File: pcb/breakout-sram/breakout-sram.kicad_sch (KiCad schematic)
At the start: 6 parts, among them J1 FX18-120P-0.8SV20, J2 FX18-120S-0.8SV20, U1 IS61WV102416DBLL-10TLI

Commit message: [pcb] misc updates prior to ordder
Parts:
- J1: Digi-Key Part Number (none) -> H11865-ND; now not fitted
- J2: Digi-Key Part Number (none) -> H11867-ND; now not fitted
- U1: LCSC Part # (none) -> C1348726
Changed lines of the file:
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@@
 		(in_bom yes)
 		(on_board yes)
-		(dnp no)
+		(dnp yes)
 		(property "Reference" "J1"
 			(at 23.876 94.488 90)
@@
 		)
 		(property "Description" ""
+			(at 41.91 96.52 0)
+			(effects
+				(font
+					(size 1.27 1.27)
+				)
+				(hide yes)
+			)
+		)
+		(property "Digi-Key Part Number" "H11865-ND"
 			(at 41.91 96.52 0)
 			(effects
@@
 		(in_bom yes)
 		(on_board yes)
-		(dnp no)
+		(dnp yes)
 		(property "Reference" "J1"
 			(at 57.658 94.488 90)
@@
 		)
 		(property "Description" ""
+			(at 76.2 96.52 0)
+			(effects
+				(font
+					(size 1.27 1.27)
+				)
+				(hide yes)
+			)
+		)
+		(property "Digi-Key Part Number" "H11865-ND"
 			(at 76.2 96.52 0)
 			(effects
@@
 		(in_bom yes)
 		(on_board yes)
-		(dnp no)
+		(dnp yes)
 		(property "Reference" "J2"
 			(at 340.868 119.126 90)
@@
 		)
 		(property "Description" ""
+			(at 356.87 96.52 0)
+			(effects
+				(font
+					(size 1.27 1.27)
+				)
+				(hide yes)
+			)
+		)
+		(property "Digi-Key Part Number" "H11867-ND"
 			(at 356.87 96.52 0)
 			(effects
@@
 			)
 		)
+		(property "LCSC Part #" " C1348726"
+			(at 208.28 125.73 0)
+			(effects
+				(font
+					(size 1.27 1.27)
+				)
+				(hide yes)
+			)
+		)
 		(pin "23"
 		)
@@
 		(in_bom yes)
 		(on_board yes)
-		(dnp no)
+		(dnp yes)
 		(property "Reference" "J2"
 			(at 307.086 120.142 90)
@@
 		)
 		(property "Description" ""
+			(at 322.58 96.52 0)
+			(effects
+				(font
+					(size 1.27 1.27)
+				)
+				(hide yes)
+			)
+		)
+		(property "Digi-Key Part Number" "H11867-ND"
 			(at 322.58 96.52 0)
 			(effects
@@
 		(in_bom yes)
 		(on_board yes)
-		(dnp no)
+		(dnp yes)
 		(property "Reference" "J1"
 			(at 94.488 94.234 90)
@@
 		)
 		(property "Description" ""
+			(at 113.03 96.52 0)
+			(effects
+				(font
+					(size 1.27 1.27)
+				)
+				(hide yes)
+			)
+		)
+		(property "Digi-Key Part Number" "H11865-ND"
 			(at 113.03 96.52 0)
 			(effects
@@
 		(in_bom yes)
 		(on_board yes)
-		(dnp no)
+		(dnp yes)
 		(property "Reference" "J2"
 			(at 377.698 119.888 90)
@@
 			(at 393.7 96.52 0)
 			(effects
+				(font
+					(size 1.27 1.27)
+				)
+				(hide yes)
+			)
+		)
+		(property "Digi-Key Part Number" "H11867-ND"
+			(at 393.7 96.52 0)
+			(effects

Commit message: [sram] update with correct nets labels
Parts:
- J1, J2: now fitted
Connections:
- net AB_02: now also J1.5, U1.46 (A7); no longer J1.4, U1.47 (A6)
- net AB_03: now also J1.7, U1.44 (OE#); no longer J1.5, U1.46 (A7)
- net AB_04: now also J1.9, U1.40 (I/O14); no longer J1.6, U1.45 (A8)
- net AB_05: now also J1.4, U1.47 (A6); no longer J1.7, U1.44 (OE#)
- net AB_06: now also J1.6, U1.45 (A8); no longer J1.8, U1.41 (I/O15)
- net AB_07: now also J1.8, U1.41 (I/O15); no longer J1.9, U1.40 (I/O14)
- net BA_02: now also J1.65, J2.5; no longer J1.64, J2.4
- net BA_03: now also J1.67, J2.7; no longer J1.65, J2.5
- net BA_04: now also J1.69, J2.9; no longer J1.66, J2.6
- net BA_05: now also J1.64, J2.4; no longer J1.67, J2.7
- net BA_06: now also J1.66, J2.6; no longer J1.68, J2.8
- net BA_07: now also J1.68, J2.8; no longer J1.69, J2.9
- net CD_02: now also J1.15, U1.34 (I/O10); no longer J1.14, U1.35 (I/O11)
- net CD_03: now also J1.17, U1.32 (I/O8); no longer J1.15, U1.34 (I/O10)
- net CD_04: now also J1.19, U1.29 (A10); no longer J1.16, U1.33 (I/O9)
- net CD_05: now also J1.14, U1.35 (I/O11); no longer J1.17, U1.32 (I/O8)
- net CD_06: now also J1.16, U1.33 (I/O9); no longer J1.18, U1.30 (A9)
- net CD_07: now also J1.18, U1.30 (A9); no longer J1.19, U1.29 (A10)
- net DC_02: now also J1.75, J2.15; no longer J1.74, J2.14
- net DC_03: now also J1.77, J2.17; no longer J1.75, J2.15
- net DC_04: now also J1.79, J2.19; no longer J1.76, J2.16
- net DC_05: now also J1.74, J2.14; no longer J1.77, J2.17
- net DC_06: now also J1.76, J2.16; no longer J1.78, J2.18
- net DC_07: now also J1.78, J2.18; no longer J1.79, J2.19
- net EF_02: now also J1.25, U1.25 (A14); no longer J1.24, U1.26 (A13)
- net EF_03: now also J1.27, U1.2 (A3); no longer J1.25, U1.25 (A14)
- net EF_04: now also J1.29, U1.4 (A1); no longer J1.26, U1.1 (A4)
- net EF_05: now also J1.24, U1.26 (A13); no longer J1.27, U1.2 (A3)
- net EF_06: now also J1.26, U1.1 (A4); no longer J1.28, U1.3 (A2)
- net EF_07: now also J1.28, U1.3 (A2); no longer J1.29, U1.4 (A1)
- net FE_01: now also J1.90, J2.30; no longer J1.83, J2.23
- net FE_02: now also J1.88, J2.28; no longer J1.84, J2.24
- net FE_03: now also J1.86, J2.26; no longer J1.85, J2.25
- net FE_04: now also J1.84, J2.24; no longer J1.86, J2.26
- net FE_05: now also J1.89, J2.29; no longer J1.87, J2.27
- net FE_06: now also J1.87, J2.27; no longer J1.88, J2.28
- net FE_07: now also J1.85, J2.25; no longer J1.89, J2.29
- net FE_08: now also J1.83, J2.23; no longer J1.90, J2.30
- net GH_02: now also J1.33, U1.9 (I/O1); no longer J1.32, U1.8 (I/O0)
- net GH_03: now also J1.35, U1.11 (I/O3); no longer J1.33, U1.9 (I/O1)
- net GH_04: now also J1.37, U1.15 (I/O5); no longer J1.34, U1.10 (I/O2)
- net GH_05: now also J1.32, U1.8 (I/O0); no longer J1.35, U1.11 (I/O3)
- net GH_06: now also J1.34, U1.10 (I/O2); no longer J1.36, U1.14 (I/O4)
- net GH_07: now also J1.36, U1.14 (I/O4); no longer J1.37, U1.15 (I/O5)
- net HG_02: now also J1.93, J2.33; no longer J1.92, J2.32
- net HG_03: now also J1.95, J2.35; no longer J1.93, J2.33
- net HG_04: now also J1.97, J2.37; no longer J1.94, J2.34
- net HG_05: now also J1.92, J2.32; no longer J1.95, J2.35
- net HG_06: now also J1.94, J2.34; no longer J1.96, J2.36
- net HG_07: now also J1.96, J2.36; no longer J1.97, J2.37
- net IJ_02: now also J1.43, U1.20 (A19); no longer J1.42, U1.18 (WE#)
- net IJ_03: now also J1.45, U1.22 (A17); no longer J1.43, U1.20 (A19)
- net IJ_04: now also J1.47, U1.24 (A15); no longer J1.44, U1.21 (A18)
- net IJ_05: now also J1.42, U1.18 (WE#); no longer J1.45, U1.22 (A17)
- net IJ_06: now also J1.44, U1.21 (A18); no longer J1.46, U1.23 (A16)
- net IJ_07: now also J1.46, U1.23 (A16); no longer J1.47, U1.24 (A15)
- net JI_01: now also J1.108, J2.48; no longer J1.101, J2.41
- net JI_02: now also J1.106, J2.46; no longer J1.102, J2.42
- net JI_03: now also J1.104, J2.44; no longer J1.103, J2.43
- net JI_04: now also J1.102, J2.42; no longer J1.104, J2.44
- net JI_05: now also J1.107, J2.47; no longer J1.105, J2.45
- net JI_06: now also J1.105, J2.45; no longer J1.106, J2.46
- net JI_07: now also J1.103, J2.43; no longer J1.107, J2.47
- net JI_08: now also J1.101, J2.41; no longer J1.108, J2.48
- net KL_02: now also J1.53, J2.113; no longer J1.52, J2.112
- net KL_03: now also J1.55, J2.115; no longer J1.53, J2.113
- net KL_04: now also J1.57, J2.117; no longer J1.54, J2.114
- net KL_05: now also J1.52, J2.112; no longer J1.55, J2.115
- net KL_06: now also J1.54, J2.114; no longer J1.56, J2.116
- net KL_07: now also J1.56, J2.116; no longer J1.57, J2.117
- net LK_02: now also J1.113, J2.53; no longer J1.112, J2.52
- net LK_03: now also J1.115, J2.55; no longer J1.113, J2.53
- net LK_04: now also J1.117, J2.57; no longer J1.114, J2.54
- net LK_05: now also J1.112, J2.52; no longer J1.115, J2.55
- net LK_06: now also J1.114, J2.54; no longer J1.116, J2.56
- net LK_07: now also J1.116, J2.56; no longer J1.117, J2.57

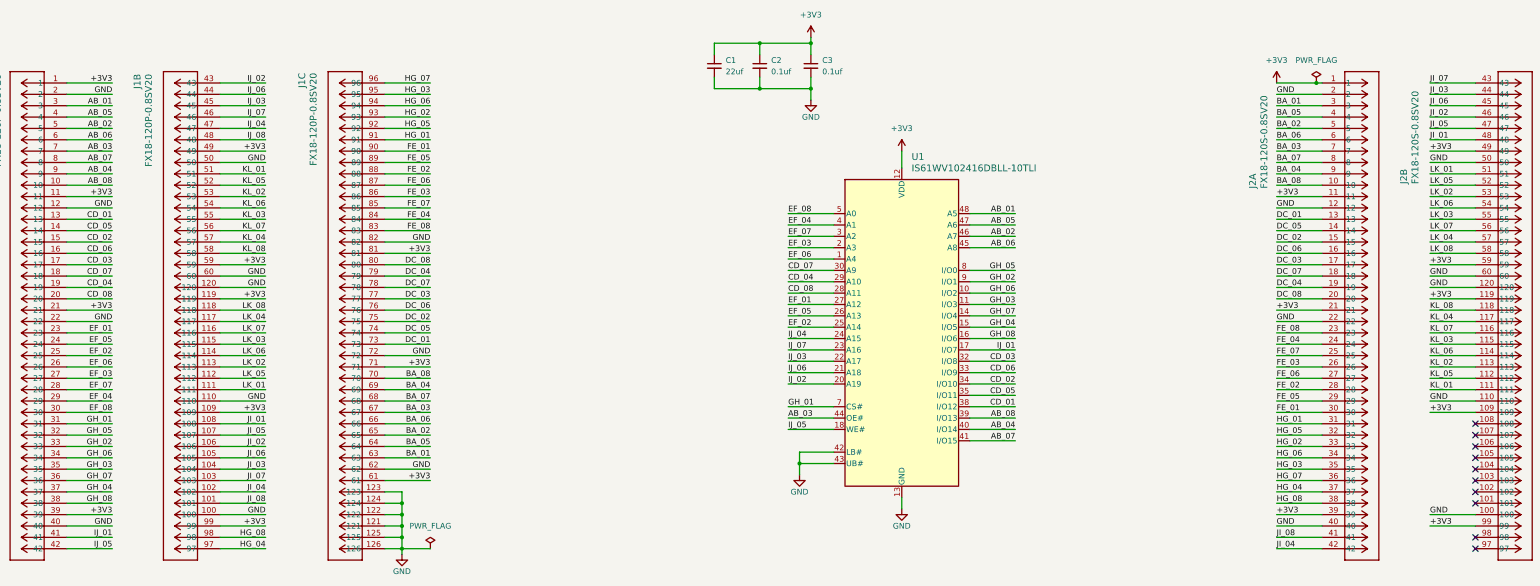
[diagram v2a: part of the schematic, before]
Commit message: [pcb][sram] switch to single letter labels
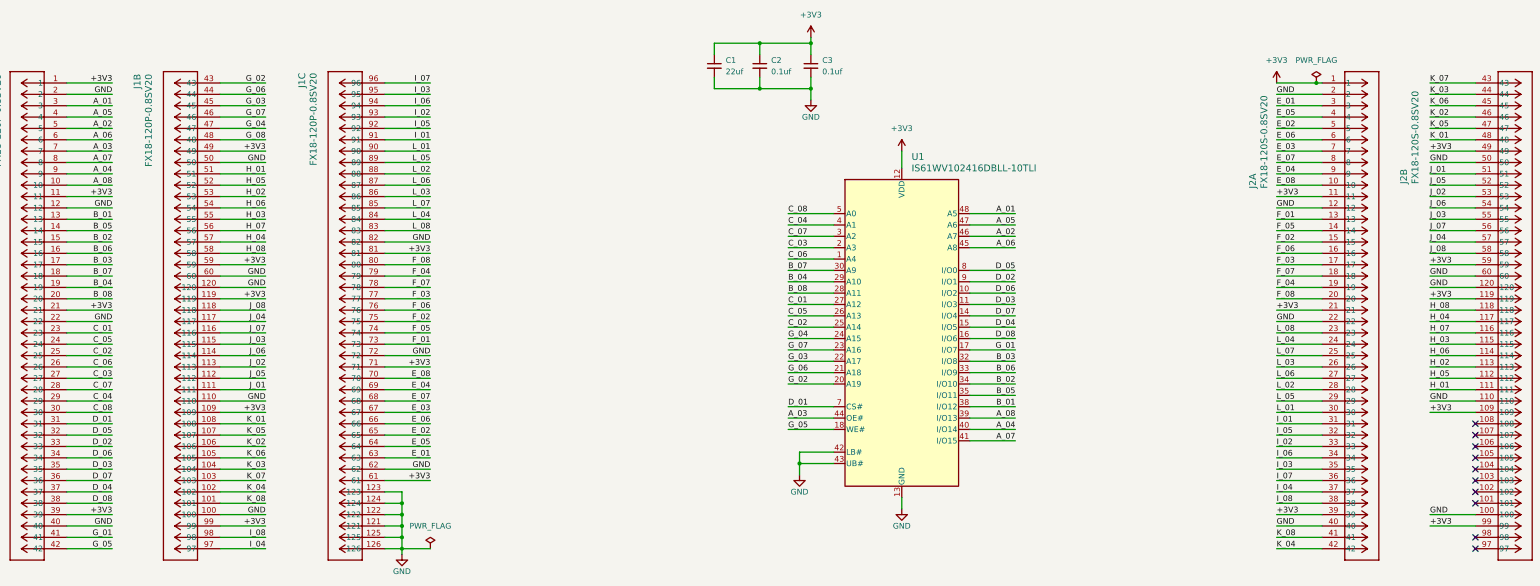
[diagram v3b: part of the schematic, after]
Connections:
- net AB_01 renamed A_01
- net AB_02 renamed A_02
- net AB_03 renamed A_03
- net AB_04 renamed A_04
- net AB_05 renamed A_05
- net AB_06 renamed A_06
- net AB_07 renamed A_07
- net AB_08 renamed A_08
- net BA_01 renamed E_01
- net BA_02 renamed E_02
- net BA_03 renamed E_03
- net BA_04 renamed E_04
- net BA_05 renamed E_05
- net BA_06 renamed E_06
- net BA_07 renamed E_07
- net BA_08 renamed E_08
- net CD_01 renamed B_01
- net CD_02 renamed B_02
- net CD_03 renamed B_03
- net CD_04 renamed B_04
- net CD_05 renamed B_05
- net CD_06 renamed B_06
- net CD_07 renamed B_07
- net CD_08 renamed B_08
- net DC_01 renamed F_01
- net DC_02 renamed F_02
- net DC_03 renamed F_03
- net DC_04 renamed F_04
- net DC_05 renamed F_05
- net DC_06 renamed F_06
- net DC_07 renamed F_07
- net DC_08 renamed F_08
- net EF_01 renamed C_01
- net EF_02 renamed C_02
- net EF_03 renamed C_03
- net EF_04 renamed C_04
- net EF_05 renamed C_05
- net EF_06 renamed C_06
- net EF_07 renamed C_07
- net EF_08 renamed C_08
- net FE_01 renamed L_01
- net FE_02 renamed L_02
- net FE_03 renamed L_03
- net FE_04 renamed L_04
- net FE_05 renamed L_05
- net FE_06 renamed L_06
- net FE_07 renamed L_07
- net FE_08 renamed L_08
- net GH_01 renamed D_01
- net GH_02 renamed D_02
- net GH_03 renamed D_03
- net GH_04 renamed D_04
- net GH_05 renamed D_05
- net GH_06 renamed D_06
- net GH_07 renamed D_07
- net GH_08 renamed D_08
- net HG_01 renamed I_01
- net HG_02 renamed I_02
- net HG_03 renamed I_03
- net HG_04 renamed I_04
- net HG_05 renamed I_05
- net HG_06 renamed I_06
- net HG_07 renamed I_07
- net HG_08 renamed I_08
- net IJ_01 renamed G_01
- net IJ_02 renamed G_02
- net IJ_03 renamed G_03
- net IJ_04 renamed G_04
- net IJ_05 renamed G_05
- net IJ_06 renamed G_06
- net IJ_07 renamed G_07
- net IJ_08 renamed G_08
- net JI_01 renamed K_01
- net JI_02 renamed K_02
- net JI_03 renamed K_03
- net JI_04 renamed K_04
- net JI_05 renamed K_05
- net JI_06 renamed K_06
- net JI_07 renamed K_07
- net JI_08 renamed K_08
- net KL_01 renamed H_01
- net KL_02 renamed H_02
- net KL_03 renamed H_03
- net KL_04 renamed H_04
- net KL_05 renamed H_05
- net KL_06 renamed H_06
- net KL_07 renamed H_07
- net KL_08 renamed H_08
- net LK_01 renamed J_01
- net LK_02 renamed J_02
- net LK_03 renamed J_03
- net LK_04 renamed J_04
- net LK_05 renamed J_05
- net LK_06 renamed J_06
- net LK_07 renamed J_07
- net LK_08 renamed J_08

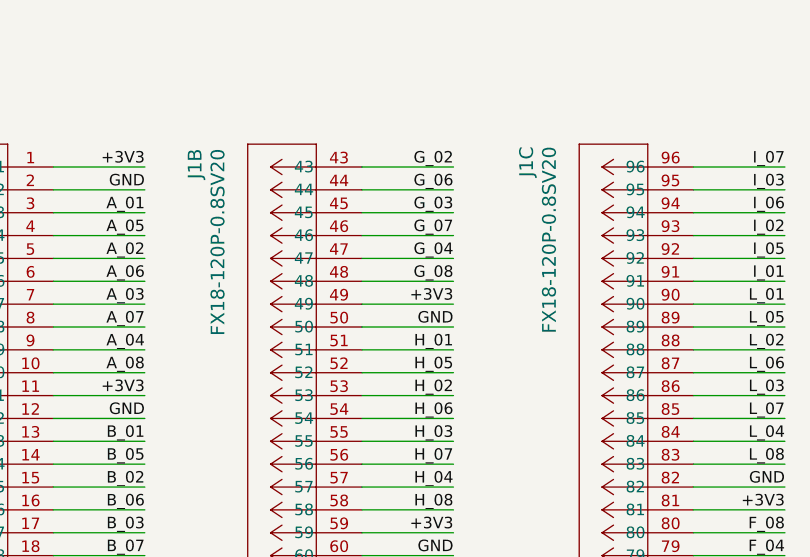
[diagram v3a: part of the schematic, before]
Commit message: [pcb][sram] tidy up routing
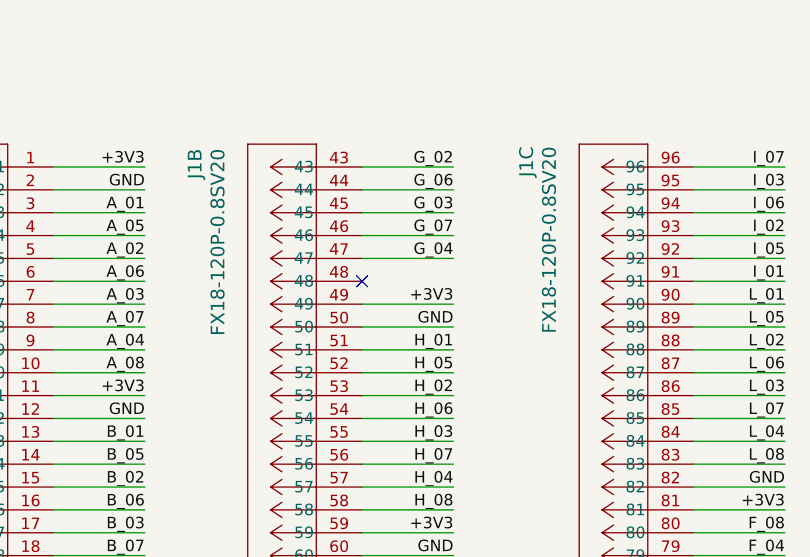
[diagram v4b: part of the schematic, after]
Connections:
- net G_08: no longer names the net of J1.48
- no-connect marks 40 -> 41
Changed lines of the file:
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@@
 	)
 	(no_connect
+		(at 76.2 109.22)
+	)
+	(no_connect
 		(at 393.7 177.8)
 	)
@@
 	(wire
 		(pts
-			(xy 86.36 109.22) (xy 76.2 109.22)
-		)
-		(stroke
-			(width 0)
-			(type default)
-		)
-	)
-	(wire
-		(pts
 			(xy 123.19 99.06) (xy 113.03 99.06)
 		)
@@
 		)
 	)
-	(label "G_08"
-		(at 86.36 109.22 180)
-		(fields_autoplaced yes)
-		(effects
-			(font
-				(size 1.27 1.27)
-			)
-			(justify right bottom)
-		)
-	)

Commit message: [pcb][pmod] remove stale ref from pcb
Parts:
- J1: LCSC Part # (none) -> C3650293
- J2: LCSC Part # (none) -> C598059
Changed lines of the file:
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@@
+			)
+		)
+		(property "LCSC Part #" "C3650293"
+			(at 41.91 96.52 0)
+			(effects
+				(font
+					(size 1.27 1.27)
+				)
+				(hide yes)
 			)
 		)
@@
 			)
 		)
+		(property "LCSC Part #" "C3650293"
+			(at 76.2 96.52 0)
+			(effects
+				(font
+					(size 1.27 1.27)
+				)
+				(hide yes)
+			)
+		)
 		(pin "9"
 		)
@@
 			)
 		)
+		(property "LCSC Part #" "C598059"
+			(at 356.87 96.52 0)
+			(effects
+				(font
+					(size 1.27 1.27)
+				)
+				(hide yes)
+			)
+		)
 		(pin "117"
 		)
@@
 			)
 		)
+		(property "LCSC Part #" "C598059"
+			(at 322.58 96.52 0)
+			(effects
+				(font
+					(size 1.27 1.27)
+				)
+				(hide yes)
+			)
+		)
 		(pin "117"
 		)
@@
 			)
 		)
+		(property "LCSC Part #" "C3650293"
+			(at 113.03 96.52 0)
+			(effects
+				(font
+					(size 1.27 1.27)
+				)
+				(hide yes)
+			)
+		)
 		(pin "9"
 		)
@@
 			(at 393.7 96.52 0)
 			(effects
+				(font
+					(size 1.27 1.27)
+				)
+				(hide yes)
+			)
+		)
+		(property "LCSC Part #" "C598059"
+			(at 393.7 96.52 0)
+			(effects

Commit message: [pcb] add FX18-120P footprint and update pcbs
and a few adc fixes, including a key resistor fix
(the op amp for Y had a copy paste error from X
on the positive Rg)
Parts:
- J1: footprint custom:CUSTOM_FX_120S-0.8SH20 -> custom:CUSTOM_FX_120P-0.8SH20
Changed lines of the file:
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@@
 	)
 	(symbol
-		(lib_name "FX18-120P-0.8SV20_1")
 		(lib_id "FX18-120P-0-8SV20:FX18-120P-0.8SV20")
 		(at 41.91 96.52 0)
@@
 			)
 		)
-		(property "Footprint" "custom:CUSTOM_FX_120S-0.8SH20"
+		(property "Footprint" "custom:CUSTOM_FX_120P-0.8SH20"
 			(at 41.91 96.52 0)
 			(effects
@@
 			)
 		)
-		(property "Footprint" "custom:CUSTOM_FX_120S-0.8SH20"
+		(property "Footprint" "custom:CUSTOM_FX_120P-0.8SH20"
 			(at 76.2 96.52 0)
 			(effects
@@
 			)
 		)
-		(property "Footprint" "custom:CUSTOM_FX_120S-0.8SH20"
+		(property "Footprint" "custom:CUSTOM_FX_120P-0.8SH20"
 			(at 113.03 96.52 0)
 			(effects
